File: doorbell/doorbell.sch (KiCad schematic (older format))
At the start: 24 parts, among them J1 39700-0012, K1 G6E-134P-US DC12, T1 CT05-1000, U1 LM2575-12WT, U2 LM358, U3 COM-16473 (NA555)

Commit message: Adding more images
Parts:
- removed D6, D7, D8: 1N5822, Diode_THT:D_DO-201AD_P15.24mm_Horizontal, symbol Diode:1N5822
- added C5: 10uF, symbol Device:C
- added D6, D7, D8: 1N5817, Diode_THT:D_DO-41_SOD81_P10.16mm_Horizontal, symbol Diode:1N5817
- added R4: 1k, symbol Device:R
- C4: value 10uF -> 0.01uF
- R2, R3: value 100k -> 10k
- RV2: value 10k -> 100k
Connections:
- net Doorbell_A2: now also T1.4 (SB); no longer T1.2 (AB)
- net GND: now also T1.1 (AA), C5.2, D7.2 (A); no longer T1.3 (SA)
- net Trans2: now also T1.3 (SA); no longer T1.1 (AA)
- net at R1.1: now also T1.2 (AB), D6.2 (A); no longer T1.4 (SB)
- net at C3.2: now also D6.1 (K)
- net at R3.2, U3.2 (TR): now also R4.1; no longer U2.1
- net at U3.3 (Q): now also D8.2 (A)
- net at RV2.3, U3.6 (THR), U3.7 (DIS): now also C5.1
- net at K1.6: now also D7.1 (K), D8.1 (K)
- new net: R4.2, U2.1
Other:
- moved on the sheet: J1, R3
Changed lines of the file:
@@
 Title "Video Doorbell Adapter"
 Date "2025-08-03"
-Rev "0.1.1"
+Rev "0.1.2"
 Comp ""
 Comment1 ""
@@
 Connection ~ 3750 1300
 $Comp
-L power:GND #PWR?
+L power:GND #PWR0101
 U 1 1 67EAEA27
 P 3100 1900
-F 0 "#PWR?" H 3100 1650 50  0001 C CNN
+F 0 "#PWR0101" H 3100 1650 50  0001 C CNN
 F 1 "GND" H 3105 1727 50  0000 C CNN
 F 2 "" H 3100 1900 50  0001 C CNN
@@
 Connection ~ 3100 1900
 $Comp
-L power:GND #PWR?
+L power:GND #PWR0102
 U 1 1 67EC0627
 P 4300 1700
-F 0 "#PWR?" H 4300 1450 50  0001 C CNN
+F 0 "#PWR0102" H 4300 1450 50  0001 C CNN
 F 1 "GND" H 4305 1527 50  0000 C CNN
 F 2 "" H 4300 1700 50  0001 C CNN
@@
 F 3 "~" H 1700 3350 50  0001 C CNN
 	1    1700 3350
-	1    0    0    -1
+	-1   0    0    1
 $EndComp
 $Comp
@@
 	2200 3150 2200 3200
 $Comp
-L power:GND #PWR?
+L power:GND #PWR0103
 U 1 1 6890211A
 P 2200 3550
-F 0 "#PWR?" H 2200 3300 50  0001 C CNN
+F 0 "#PWR0103" H 2200 3300 50  0001 C CNN
 F 1 "GND" H 2205 3377 50  0000 C CNN
 F 2 "" H 2200 3550 50  0001 C CNN
@@
 	3200 3150 3400 3150
 $Comp
-L power:GND #PWR?
+L power:GND #PWR0104
 U 1 1 689136EB
 P 3650 2800
-F 0 "#PWR?" H 3650 2550 50  0001 C CNN
+F 0 "#PWR0104" H 3650 2550 50  0001 C CNN
 F 1 "GND" H 3655 2627 50  0000 C CNN
 F 2 "" H 3650 2800 50  0001 C CNN
@@
 P 7050 2850
 F 0 "RV2" H 6980 2896 50  0000 R CNN
-F 1 "10k" H 6980 2805 50  0000 R CNN
+F 1 "100k" H 6980 2805 50  0000 R CNN
 F 2 "" H 7050 2850 50  0001 C CNN
 F 3 "~" H 7050 2850 50  0001 C CNN
@@
 L Device:R R3
 U 1 1 68921E19
-P 5300 2800
-F 0 "R3" H 5370 2846 50  0000 L CNN
-F 1 "100k" H 5370 2755 50  0000 L CNN
-F 2 "" V 5230 2800 50  0001 C CNN
-F 3 "~" H 5300 2800 50  0001 C CNN
-	1    5300 2800
+P 5200 2800
+F 0 "R3" H 5270 2846 50  0000 L CNN
+F 1 "10k" H 5270 2755 50  0000 L CNN
+F 2 "" V 5130 2800 50  0001 C CNN
+F 3 "~" H 5200 2800 50  0001 C CNN
+	1    5200 2800
 	1    0    0    -1
 $EndComp
@@
 	6000 2600 5450 2600
 Wire Wire Line
-	5300 2600 5300 2650
-Wire Wire Line
-	5300 2950 5300 3050
-Wire Wire Line
-	5300 3050 5500 3050
-Wire Wire Line
-	5300 3050 4600 3050
-Connection ~ 5300 3050
-Wire Wire Line
 	5450 2600 5450 3450
 Wire Wire Line
 	5450 3450 5500 3450
-Connection ~ 5450 2600
-Wire Wire Line
-	5450 2600 5300 2600
-$Comp
-L power:GND #PWR?
+$Comp
+L power:GND #PWR0105
 U 1 1 6892671A
 P 5300 3800
-F 0 "#PWR?" H 5300 3550 50  0001 C CNN
+F 0 "#PWR0105" H 5300 3550 50  0001 C CNN
 F 1 "GND" H 5305 3627 50  0000 C CNN
 F 2 "" H 5300 3800 50  0001 C CNN
@@
 $EndComp
 $Comp
-L power:GND #PWR?
+L power:GND #PWR0106
 U 1 1 68926BDF
 P 6000 3800
-F 0 "#PWR?" H 6000 3550 50  0001 C CNN
+F 0 "#PWR0106" H 6000 3550 50  0001 C CNN
 F 1 "GND" H 6005 3627 50  0000 C CNN
 F 2 "" H 6000 3800 50  0001 C CNN
@@
 Connection ~ 4300 1300
 $Comp
-L power:GND #PWR?
+L power:GND #PWR0107
 U 1 1 68941A41
 P 5500 1800
-F 0 "#PWR?" H 5500 1550 50  0001 C CNN
+F 0 "#PWR0107" H 5500 1550 50  0001 C CNN
 F 1 "GND" H 5505 1627 50  0000 C CNN
 F 2 "" H 5500 1800 50  0001 C CNN
@@
 12V
 $Comp
-L Diode:1N5822 D6
-U 1 1 6896EDE9
-P 2600 3150
-F 0 "D6" H 2600 2934 50  0000 C CNN
-F 1 "1N5822" H 2600 3025 50  0000 C CNN
-F 2 "Diode_THT:D_DO-201AD_P15.24mm_Horizontal" H 2600 2975 50  0001 C CNN
-F 3 "http://www.vishay.com/docs/88526/1n5820.pdf" H 2600 3150 50  0001 C CNN
-	1    2600 3150
-	-1   0    0    1
-$EndComp
-$Comp
 L Device:R R2
 U 1 1 6896F886
 P 3400 3300
 F 0 "R2" H 3470 3346 50  0000 L CNN
-F 1 "100k" H 3470 3255 50  0000 L CNN
+F 1 "10k" H 3470 3255 50  0000 L CNN
 F 2 "" V 3330 3300 50  0001 C CNN
 F 3 "~" H 3400 3300 50  0001 C CNN
@@
 	3400 3150 4000 3150
 $Comp
-L power:GND #PWR?
+L power:GND #PWR0108
 U 1 1 6897012F
 P 3400 3450
-F 0 "#PWR?" H 3400 3200 50  0001 C CNN
+F 0 "#PWR0108" H 3400 3200 50  0001 C CNN
 F 1 "GND" H 3405 3277 50  0000 C CNN
 F 2 "" H 3400 3450 50  0001 C CNN
@@
 L Connector:Screw_Terminal_01x12 J1
 U 1 1 68992D80
-P 1100 4950
-F 0 "J1" H 1018 4125 50  0000 C CNN
-F 1 "39700-0012 " H 1018 4216 50  0000 C CNN
-F 2 "" H 1100 4950 50  0001 C CNN
-F 3 "~" H 1100 4950 50  0001 C CNN
-	1    1100 4950
+P 2700 5350
+F 0 "J1" H 2618 4525 50  0000 C CNN
+F 1 "39700-0012 " H 2618 4616 50  0000 C CNN
+F 2 "" H 2700 5350 50  0001 C CNN
+F 3 "~" H 2700 5350 50  0001 C CNN
+	1    2700 5350
 	-1   0    0    1
 $EndComp
-Text GLabel 1600 5450 2    50   Input ~ 0
+Text GLabel 3200 5850 2    50   Input ~ 0
 Trans1
-Text GLabel 1600 5350 2    50   Input ~ 0
+Text GLabel 3200 5750 2    50   Input ~ 0
 Trans2
-Text GLabel 1600 5250 2    50   Input ~ 0
+Text GLabel 3200 5650 2    50   Input ~ 0
 Doorbell_A1
-Text GLabel 1600 5150 2    50   Input ~ 0
+Text GLabel 3200 5550 2    50   Input ~ 0
 Doorbell_A2
-Text GLabel 1600 5050 2    50   Input ~ 0
+Text GLabel 3200 5450 2    50   Input ~ 0
 Doorbell_B1
-Text GLabel 1600 4950 2    50   Input ~ 0
+Text GLabel 3200 5350 2    50   Input ~ 0
 Doorbell_B2
-Text GLabel 1600 4850 2    50   Input ~ 0
+Text GLabel 3200 5250 2    50   Input ~ 0
 Doorbell_C1
-Text GLabel 1600 4750 2    50   Input ~ 0
+Text GLabel 3200 5150 2    50   Input ~ 0
 Doorbell_C2
-Text GLabel 1600 4650 2    50   Input ~ 0
+Text GLabel 3200 5050 2    50   Input ~ 0
 Chime_Common
-Text GLabel 1600 4550 2    50   Input ~ 0
+Text GLabel 3200 4950 2    50   Input ~ 0
 Chime_A
-Text GLabel 1600 4450 2    50   Input ~ 0
+Text GLabel 3200 4850 2    50   Input ~ 0
 Chime_B
-Text GLabel 1600 4350 2    50   Input ~ 0
+Text GLabel 3200 4750 2    50   Input ~ 0
 Chime_C
 Wire Wire Line
-	1300 4350 1600 4350
-Wire Wire Line
-	1300 4450 1600 4450
-Wire Wire Line
-	1300 4550 1600 4550
-Wire Wire Line
-	1300 4650 1600 4650
-Wire Wire Line
-	1300 4750 1600 4750
-Wire Wire Line
-	1300 4850 1600 4850
-Wire Wire Line
-	1300 4950 1600 4950
-Wire Wire Line
-	1300 5050 1600 5050
-Wire Wire Line
-	1300 5150 1600 5150
-Wire Wire Line
-	1300 5250 1600 5250
-Wire Wire Line
-	1300 5350 1600 5350
-Wire Wire Line
-	1300 5450 1600 5450
+	2900 4750 3200 4750
+Wire Wire Line
+	2900 4850 3200 4850
+Wire Wire Line
+	2900 4950 3200 4950
+Wire Wire Line
+	2900 5050 3200 5050
+Wire Wire Line
+	2900 5150 3200 5150
+Wire Wire Line
+	2900 5250 3200 5250
+Wire Wire Line
+	2900 5350 3200 5350
+Wire Wire Line
+	2900 5450 3200 5450
+Wire Wire Line
+	2900 5550 3200 5550
+Wire Wire Line
+	2900 5650 3200 5650
+Wire Wire Line
+	2900 5750 3200 5750
+Wire Wire Line
+	2900 5850 3200 5850
 Text GLabel 1200 3550 0    50   Input ~ 0
 Doorbell_A2
@@
 	8800 3050 8800 3100
 $Comp
-L power:GND #PWR?
+L power:GND #PWR0109
 U 1 1 6894DFDB
 P 8800 3800
-F 0 "#PWR?" H 8800 3550 50  0001 C CNN
+F 0 "#PWR0109" H 8800 3550 50  0001 C CNN
 F 1 "GND" H 8805 3627 50  0000 C CNN
 F 2 "" H 8800 3800 50  0001 C CNN
@@
 $EndComp
 $Comp
-L power:GND #PWR?
+L power:GND #PWR0110
 U 1 1 689581AF
 P 7700 3800
-F 0 "#PWR?" H 7700 3550 50  0001 C CNN
+F 0 "#PWR0110" H 7700 3550 50  0001 C CNN
 F 1 "GND" H 7705 3627 50  0000 C CNN
 F 2 "" H 7700 3800 50  0001 C CNN
@@
 Wire Wire Line
 	6000 2350 6000 2600
-$Comp
-L Diode:1N5822 D8
-U 1 1 68977B36
-P 7500 3050
-F 0 "D8" H 7500 2834 50  0000 C CNN
-F 1 "1N5822" H 7500 2925 50  0000 C CNN
-F 2 "Diode_THT:D_DO-201AD_P15.24mm_Horizontal" H 7500 2875 50  0001 C CNN
-F 3 "http://www.vishay.com/docs/88526/1n5820.pdf" H 7500 3050 50  0001 C CNN
-	1    7500 3050
-	-1   0    0    1
-$EndComp
-$Comp
-L Diode:1N5822 D7
-U 1 1 6897B19A
-P 7700 3500
-F 0 "D7" H 7700 3284 50  0000 C CNN
-F 1 "1N5822" H 7700 3375 50  0000 C CNN
-F 2 "Diode_THT:D_DO-201AD_P15.24mm_Horizontal" H 7700 3325 50  0001 C CNN
-F 3 "http://www.vishay.com/docs/88526/1n5820.pdf" H 7700 3500 50  0001 C CNN
-	1    7700 3500
-	0    1    1    0
-$EndComp
 Wire Wire Line
 	1200 2150 3750 2150
@@
 P 5300 3550
 F 0 "C4" H 5415 3596 50  0000 L CNN
-F 1 "10uF" H 5415 3505 50  0000 L CNN
+F 1 "0.01uF" H 5415 3505 50  0000 L CNN
 F 2 "" H 5338 3400 50  0001 C CNN
 F 3 "~" H 5300 3550 50  0001 C CNN
@@
 	1    0    0    -1
 $EndComp
+$Comp
+L Diode:1N5817 D6
+U 1 1 68995277
+P 2600 3150
+F 0 "D6" H 2600 2934 50  0000 C CNN
+F 1 "1N5817" H 2600 3025 50  0000 C CNN
+F 2 "Diode_THT:D_DO-41_SOD81_P10.16mm_Horizontal" H 2600 2975 50  0001 C CNN
+F 3 "http://www.vishay.com/docs/88525/1n5817.pdf" H 2600 3150 50  0001 C CNN
+	1    2600 3150
+	-1   0    0    1
+$EndComp
+$Comp
+L Diode:1N5817 D8
+U 1 1 689A1084
+P 7500 3050
+F 0 "D8" H 7500 2834 50  0000 C CNN
+F 1 "1N5817" H 7500 2925 50  0000 C CNN
+F 2 "Diode_THT:D_DO-41_SOD81_P10.16mm_Horizontal" H 7500 2875 50  0001 C CNN
+F 3 "http://www.vishay.com/docs/88525/1n5817.pdf" H 7500 3050 50  0001 C CNN
+	1    7500 3050
+	-1   0    0    1
+$EndComp
+$Comp
+L Diode:1N5817 D7
+U 1 1 689A2011
+P 7700 3500
+F 0 "D7" V 7654 3579 50  0000 L CNN
+F 1 "1N5817" V 7745 3579 50  0000 L CNN
+F 2 "Diode_THT:D_DO-41_SOD81_P10.16mm_Horizontal" H 7700 3325 50  0001 C CNN
+F 3 "http://www.vishay.com/docs/88525/1n5817.pdf" H 7700 3500 50  0001 C CNN
+	1    7700 3500
+	0    1    1    0
+$EndComp
+$Comp
+L Device:C C5
+U 1 1 689A5EB1
+P 7050 3600
+F 0 "C5" H 7165 3646 50  0000 L CNN
+F 1 "10uF" H 7165 3555 50  0000 L CNN
+F 2 "" H 7088 3450 50  0001 C CNN
+F 3 "~" H 7050 3600 50  0001 C CNN
+	1    7050 3600
+	1    0    0    -1
+$EndComp
+Connection ~ 7050 3450
+$Comp
+L Device:R R4
+U 1 1 689A7583
+P 4900 3050
+F 0 "R4" V 4693 3050 50  0000 C CNN
+F 1 "1k" V 4784 3050 50  0000 C CNN
+F 2 "" V 4830 3050 50  0001 C CNN
+F 3 "~" H 4900 3050 50  0001 C CNN
+	1    4900 3050
+	0    1    1    0
+$EndComp
+$Comp
+L power:GND #PWR0111
+U 1 1 689A8CD2
+P 7050 3800
+F 0 "#PWR0111" H 7050 3550 50  0001 C CNN
+F 1 "GND" H 7055 3627 50  0000 C CNN
+F 2 "" H 7050 3800 50  0001 C CNN
+F 3 "" H 7050 3800 50  0001 C CNN
+	1    7050 3800
+	1    0    0    -1
+$EndComp
+Wire Wire Line
+	7050 3750 7050 3800
+Wire Wire Line
+	5450 2600 5200 2600
+Wire Wire Line
+	5200 2600 5200 2650
+Connection ~ 5450 2600
+Wire Wire Line
+	5200 2950 5200 3050
+Connection ~ 5200 3050
+Wire Wire Line
+	5200 3050 5500 3050
+Wire Wire Line
+	4600 3050 4750 3050
+Wire Wire Line
+	5050 3050 5200 3050
 $EndSCHEMATC

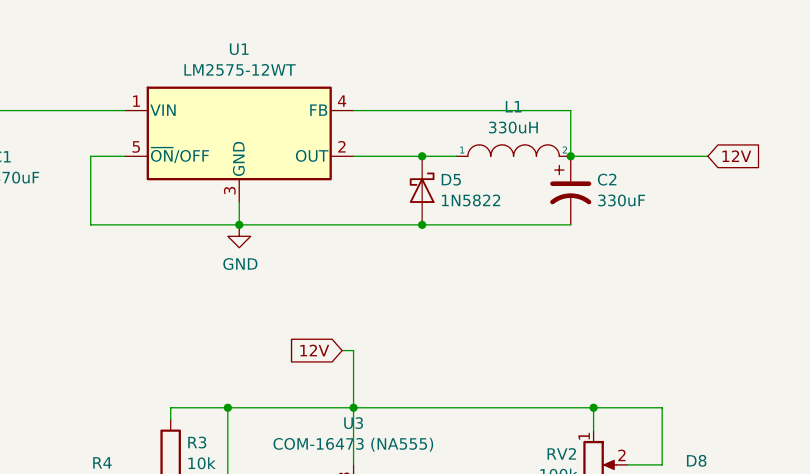
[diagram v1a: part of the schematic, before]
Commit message: v0.1.3 - adjusted some diodes. Updated readme
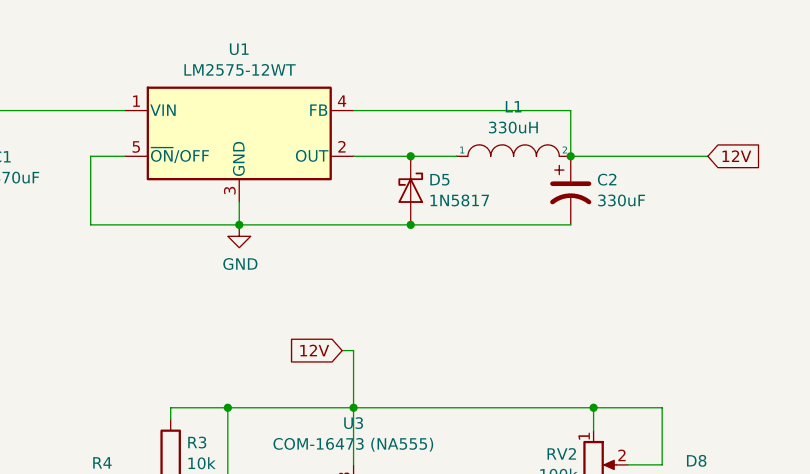
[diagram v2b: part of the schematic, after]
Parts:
- removed D5: 1N5822, Diode_THT:D_DO-201AD_P15.24mm_Horizontal, symbol Diode:1N5822
- added D5: 1N5817, Diode_THT:D_DO-41_SOD81_P10.16mm_Horizontal, symbol Diode:1N5817
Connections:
- net GND: now also D5.2 (A)
- net at L1.1, U1.2 (OUT): now also D5.1 (K)
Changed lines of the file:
@@
 Sheet 1 1
 Title "Video Doorbell Adapter"
-Date "2025-08-03"
-Rev "0.1.2"
+Date "2025-08-22"
+Rev "0.1.3"
 Comp ""
 Comment1 ""
@@
 $EndComp
 $Comp
-L Diode:1N5822 D5
-U 1 1 689428CB
-P 6300 1650
-F 0 "D5" V 6254 1729 50  0000 L CNN
-F 1 "1N5822" V 6345 1729 50  0000 L CNN
-F 2 "Diode_THT:D_DO-201AD_P15.24mm_Horizontal" H 6300 1475 50  0001 C CNN
-F 3 "http://www.vishay.com/docs/88526/1n5820.pdf" H 6300 1650 50  0001 C CNN
-	1    6300 1650
-	0    1    1    0
-$EndComp
-$Comp
 L pspice:INDUCTOR L1
 U 1 1 68943E11
@@
 $EndComp
 Wire Wire Line
-	6000 1500 6300 1500
-Wire Wire Line
-	6450 1500 6300 1500
-Connection ~ 6300 1500
-Wire Wire Line
 	5500 1700 5500 1800
-Wire Wire Line
-	6300 1800 5500 1800
 Connection ~ 5500 1800
 $Comp
@@
 	6950 1300 6950 1500
 Connection ~ 6950 1500
-Wire Wire Line
-	6950 1800 6300 1800
-Connection ~ 6300 1800
 Text GLabel 7550 1500 2    50   Input ~ 0
 12V
@@
 Wire Wire Line
 	5050 3050 5200 3050
+Wire Wire Line
+	6000 1500 6250 1500
+Wire Wire Line
+	5500 1800 6250 1800
+$Comp
+L Diode:1N5817 D5
+U 1 1 68A8FA0D
+P 6250 1650
+F 0 "D5" V 6204 1729 50  0000 L CNN
+F 1 "1N5817" V 6295 1729 50  0000 L CNN
+F 2 "Diode_THT:D_DO-41_SOD81_P10.16mm_Horizontal" H 6250 1475 50  0001 C CNN
+F 3 "http://www.vishay.com/docs/88525/1n5817.pdf" H 6250 1650 50  0001 C CNN
+	1    6250 1650
+	0    1    1    0
+$EndComp
+Connection ~ 6250 1500
+Wire Wire Line
+	6250 1500 6450 1500
+Connection ~ 6250 1800
+Wire Wire Line
+	6250 1800 6950 1800
 $EndSCHEMATC

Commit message: Updating readme and peak detector
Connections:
- net GND: now also C3.2
- net at C3.1, R2.1, U2.2 (-): now also D6.1 (K)
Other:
- moved on the sheet: C3
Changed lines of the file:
@@
 L Device:C C3
 U 1 1 689051AE
-P 3050 3150
-F 0 "C3" V 2798 3150 50  0000 C CNN
-F 1 "10uF" V 2889 3150 50  0000 C CNN
-F 2 "" H 3088 3000 50  0001 C CNN
-F 3 "~" H 3050 3150 50  0001 C CNN
-	1    3050 3150
-	0    1    1    0
-$EndComp
-Wire Wire Line
-	2750 3150 2900 3150
+P 3050 3300
+F 0 "C3" V 2798 3300 50  0000 C CNN
+F 1 "10uF" V 2889 3300 50  0000 C CNN
+F 2 "" H 3088 3150 50  0001 C CNN
+F 3 "~" H 3050 3300 50  0001 C CNN
+	1    3050 3300
+	1    0    0    -1
+$EndComp
 $Comp
 L Device:R_POT RV1
@@
 	1    0    0    -1
 $EndComp
-Wire Wire Line
-	3200 3150 3400 3150
 $Comp
 L power:GND #PWR0104
@@
 	1    0    0    -1
 $EndComp
-Connection ~ 3400 3150
 Wire Wire Line
 	3400 3150 4000 3150
@@
 Wire Wire Line
 	6250 1800 6950 1800
+Wire Wire Line
+	2750 3150 3050 3150
+Connection ~ 3050 3150
+Wire Wire Line
+	3400 3150 3050 3150
+Connection ~ 3400 3150
+Wire Wire Line
+	3050 3450 3400 3450
+Connection ~ 3400 3450
 $EndSCHEMATC
